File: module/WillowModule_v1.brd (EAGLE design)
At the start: 101.6 x 47 mm, 15 parts, among them U1 SN74LV245

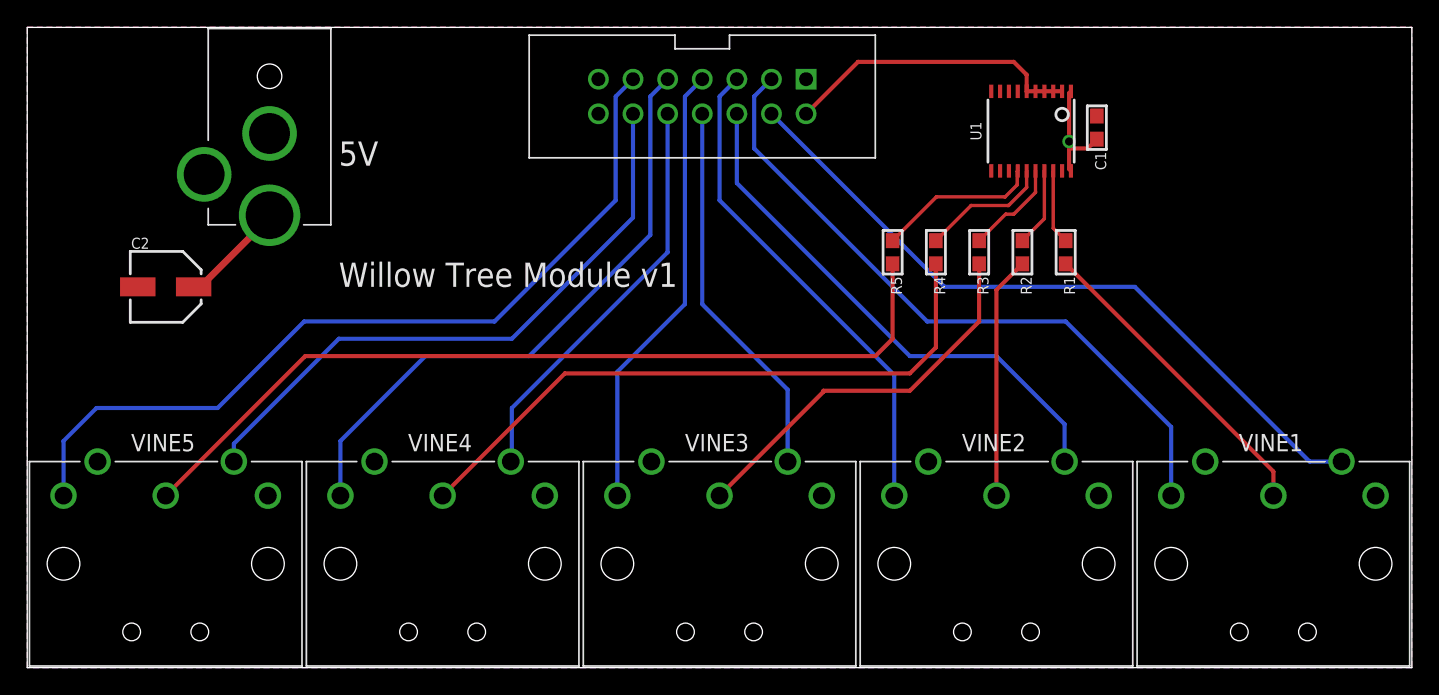
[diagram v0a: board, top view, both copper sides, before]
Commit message: Added mounting holes
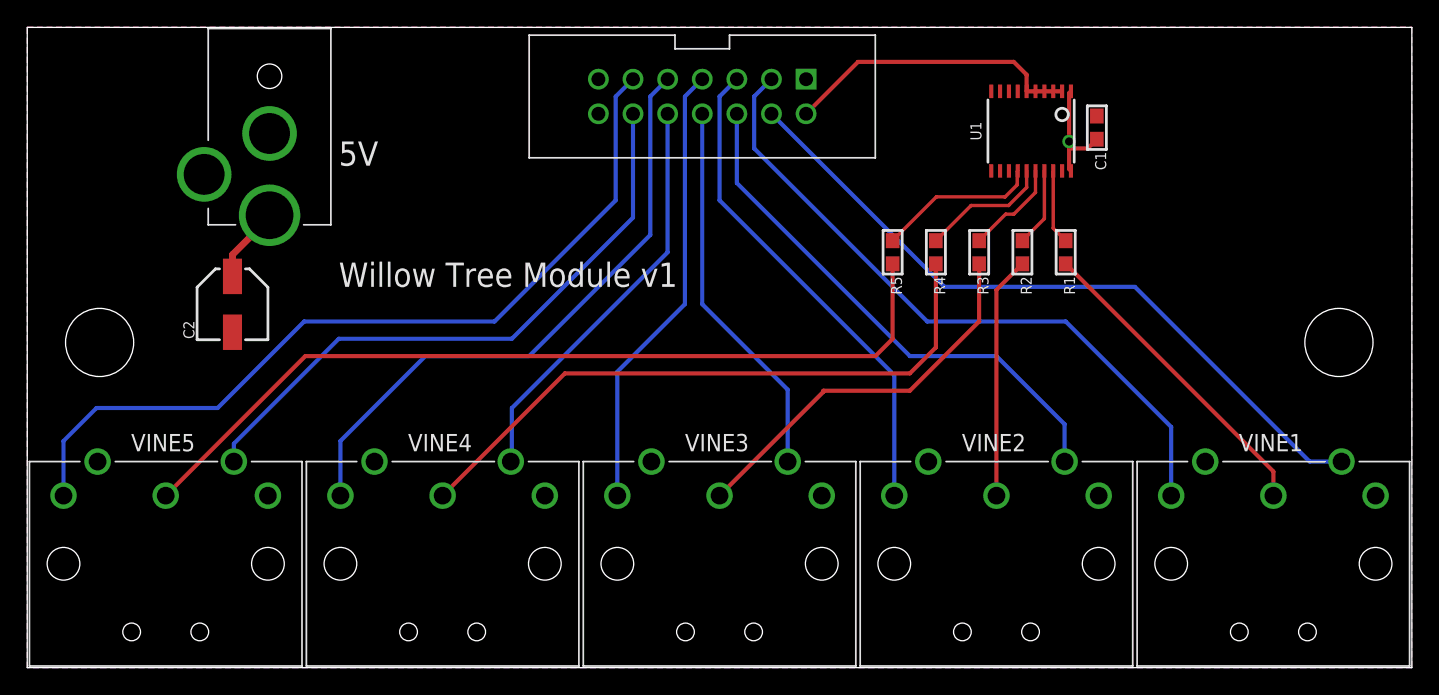
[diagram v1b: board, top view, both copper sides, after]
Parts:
- moved C2 5.06 mm to (15.1, 26.7), turned to 90 degrees
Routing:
- net VCC: track 7.36 -> 5.61 mm
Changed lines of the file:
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@@
 <setting verticaltext="up"/>
 </settings>
-<grid distance="0.05" unitdist="inch" unit="inch" style="lines" multiple="1" display="yes" altdistance="0.005" altunitdist="inch" altunit="inch"/>
+<grid distance="0.1" unitdist="inch" unit="inch" style="lines" multiple="1" display="yes" altdistance="0.5" altunitdist="mm" altunit="mm"/>
 <layers>
 <layer number="1" name="Top" color="4" fill="1" visible="yes" active="yes"/>
@@
 <layer number="43" name="vRestrict" color="2" fill="10" visible="no" active="yes"/>
 <layer number="44" name="Drills" color="7" fill="1" visible="no" active="yes"/>
-<layer number="45" name="Holes" color="7" fill="1" visible="no" active="yes"/>
+<layer number="45" name="Holes" color="7" fill="1" visible="yes" active="yes"/>
 <layer number="46" name="Milling" color="3" fill="1" visible="no" active="yes"/>
 <layer number="47" name="Measures" color="7" fill="1" visible="no" active="yes"/>
@@
 <text x="22.86" y="27.94" size="1.778" layer="21">Willow Tree Module v1</text>
 <text x="22.86" y="36.83" size="1.778" layer="21">5V</text>
+<hole x="5.31" y="23.86" drill="5"/>
+<hole x="96.25" y="23.86" drill="5"/>
 </plain>
 <attributes>
@@
 <elements>
 <element name="C1" library="microbuilder" package="0603" value="0.1uF" x="78.486" y="39.624" rot="R270"/>
-<element name="C2" library="microbuilder" package="PANASONIC_C" value="47uF" x="10.16" y="27.94"/>
+<element name="C2" library="microbuilder" package="PANASONIC_C" value="47uF" x="15.06" y="26.66" rot="R90"/>
 <element name="JP1" library="Custom" package="IDC-BOX-HEADER" value="" x="49.53" y="41.91" rot="R180"/>
 <element name="R1" library="microbuilder" package="0603" value="" x="76.2" y="30.48" rot="R270"/>
@@
 </polygon>
 <wire x1="17.78" y1="33.195" x2="17.78" y2="33.02" width="0.508" layer="1"/>
-<wire x1="17.78" y1="33.02" x2="12.7" y2="27.94" width="0.508" layer="1"/>
-<wire x1="12.7" y1="27.94" x2="12.21" y2="27.94" width="0" layer="19" extent="1-1"/>
+<wire x1="15.06" y1="28.71" x2="15.06" y2="30.3" width="0.508" layer="1"/>
+<wire x1="15.06" y1="30.3" x2="17.78" y2="33.02" width="0.508" layer="1"/>
 </signal>
 <signal name="CLK1">
